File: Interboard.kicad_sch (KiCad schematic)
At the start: 1 part

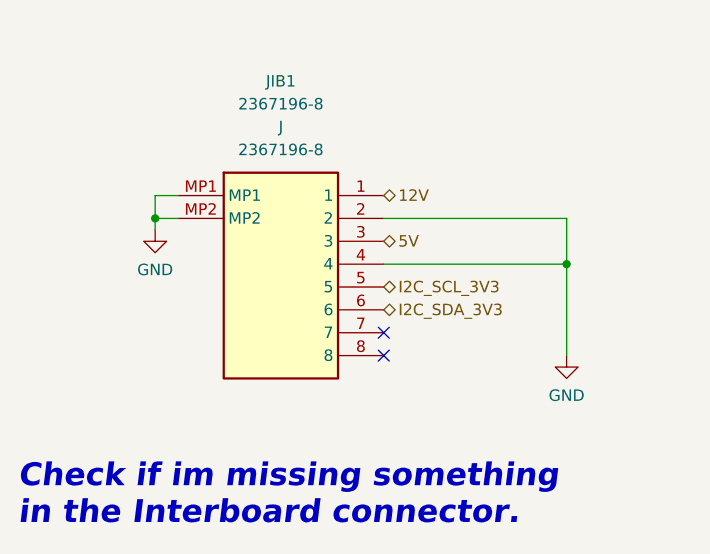
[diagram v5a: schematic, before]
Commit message: Page settings changed. Added some testpoints. Some comments are made.
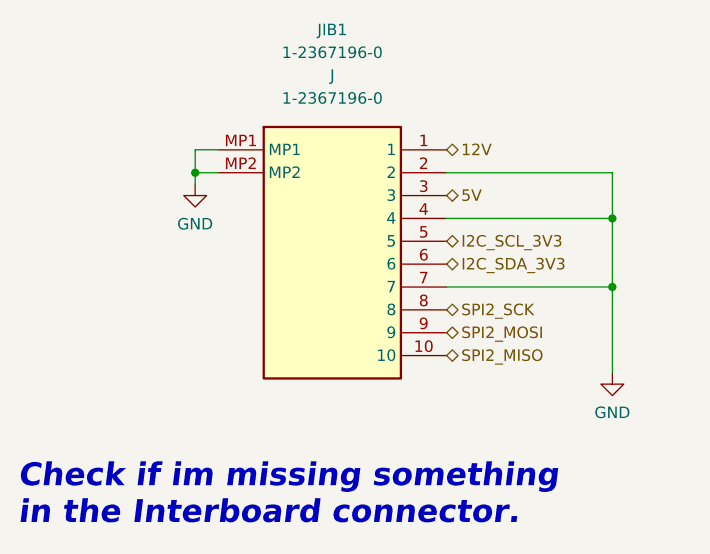
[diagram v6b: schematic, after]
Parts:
- removed JIB1: 2367196-8, symbol 2367196-8:2367196-8
- added JIB1: 1-2367196-0, symbol 1-2367196-0:1-2367196-0
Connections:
- net 12V: now also JIB1.1
- net 5V: now also JIB1.3
- net GND: now also JIB1.2, JIB1.4, JIB1.7, JIB1.MP1, JIB1.MP2
- net I2C_SCL_3V3: now also JIB1.5
- net I2C_SDA_3V3: now also JIB1.6
- new net SPI2_MISO: JIB1.10
- new net SPI2_MOSI: JIB1.9
- new net SPI2_SCK: JIB1.8
- no-connect marks 2 -> 0
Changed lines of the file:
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@@
     (company "Parikshit Student Satellite Team")
   )
-  (junction (at 162.56 86.36) (diameter 0) (color 0 0 0 0)
+  (junction (at 121.285 76.2) (diameter 0) (color 0 0 0 0)
   )
-  (junction (at 116.84 81.28) (diameter 0) (color 0 0 0 0)
+  (junction (at 167.64 88.9) (diameter 0) (color 0 0 0 0)
   )
-  (no_connect (at 142.24 93.98))
-  (no_connect (at 142.24 96.52))
-  (wire (pts (xy 116.84 81.28) (xy 116.84 82.55))
+  (junction (at 167.64 81.28) (diameter 0) (color 0 0 0 0)
+  )
+  (wire (pts (xy 121.285 76.2) (xy 121.285 77.47))
     (stroke (width 0) (type default) (color 0 0 0 0))
   )
-  (wire (pts (xy 119.38 78.74) (xy 116.84 78.74))
+  (wire (pts (xy 149.225 76.2) (xy 167.64 76.2))
     (stroke (width 0) (type default) (color 0 0 0 0))
   )
-  (wire (pts (xy 162.56 81.28) (xy 162.56 86.36))
+  (wire (pts (xy 167.64 76.2) (xy 167.64 81.28))
     (stroke (width 0) (type default) (color 0 0 0 0))
   )
-  (wire (pts (xy 142.24 86.36) (xy 162.56 86.36))
+  (wire (pts (xy 167.64 88.9) (xy 167.64 98.425))
     (stroke (width 0) (type default) (color 0 0 0 0))
   )
-  (wire (pts (xy 116.84 81.28) (xy 119.38 81.28))
+  (wire (pts (xy 167.64 81.28) (xy 167.64 88.9))
     (stroke (width 0) (type default) (color 0 0 0 0))
   )
-  (wire (pts (xy 116.84 78.74) (xy 116.84 81.28))
+  (wire (pts (xy 149.225 81.28) (xy 167.64 81.28))
     (stroke (width 0) (type default) (color 0 0 0 0))
   )
-  (wire (pts (xy 142.24 81.28) (xy 162.56 81.28))
+  (wire (pts (xy 123.825 73.66) (xy 121.285 73.66))
     (stroke (width 0) (type default) (color 0 0 0 0))
   )
-  (wire (pts (xy 162.56 86.36) (xy 162.56 96.52))
+  (wire (pts (xy 121.285 76.2) (xy 123.825 76.2))
+    (stroke (width 0) (type default) (color 0 0 0 0))
+  )
+  (wire (pts (xy 121.285 73.66) (xy 121.285 76.2))
+    (stroke (width 0) (type default) (color 0 0 0 0))
+  )
+  (wire (pts (xy 149.225 88.9) (xy 167.64 88.9))
     (stroke (width 0) (type default) (color 0 0 0 0))
   )
@@
     (effects (font (size 2.54 2.54) (thickness 0.508) bold italic) (justify left bottom))
   )
-  (hierarchical_label "12V" (shape bidirectional) (at 142.24 78.74 0)
+  (hierarchical_label "5V" (shape bidirectional) (at 149.225 78.74 0)
     (effects (font (size 1.27 1.27)) (justify left))
   )
-  (hierarchical_label "I2C_SCL_3V3" (shape bidirectional) (at 142.24 88.9 0)
+  (hierarchical_label "12V" (shape bidirectional) (at 149.225 73.66 0)
     (effects (font (size 1.27 1.27)) (justify left))
   )
-  (hierarchical_label "I2C_SDA_3V3" (shape bidirectional) (at 142.24 91.44 0)
+  (hierarchical_label "I2C_SCL_3V3" (shape bidirectional) (at 149.225 83.82 0)
     (effects (font (size 1.27 1.27)) (justify left))
   )
-  (hierarchical_label "5V" (shape bidirectional) (at 142.24 83.82 0)
+  (hierarchical_label "SPI2_MOSI" (shape bidirectional) (at 149.225 93.98 0)
     (effects (font (size 1.27 1.27)) (justify left))
   )
-  (symbol (lib_id "upsat-comms-hardware:GND") (at 162.56 96.52 0) (unit 1)
+  (hierarchical_label "SPI2_SCK" (shape bidirectional) (at 149.225 91.44 0)
+    (effects (font (size 1.27 1.27)) (justify left))
+  )
+  (hierarchical_label "I2C_SDA_3V3" (shape bidirectional) (at 149.225 86.36 0)
+    (effects (font (size 1.27 1.27)) (justify left))
+  )
+  (hierarchical_label "SPI2_MISO" (shape bidirectional) (at 149.225 96.52 0)
+    (effects (font (size 1.27 1.27)) (justify left))
+  )
+  (symbol (lib_id "1-2367196-0:1-2367196-0") (at 123.825 73.66 0) (unit 1)
     (in_bom yes) (on_board yes) (fields_autoplaced)
-    (property "Reference" "#PWR0149" (id 0) (at 162.56 102.87 0)
+    (property "Reference" "JIB1" (id 0) (at 136.525 60.325 0))
+    (property "Value" "1-2367196-0" (id 1) (at 136.525 62.865 0))
+    (property "Footprint" "" (id 2) (at 123.825 73.66 0)
       (effects (font (size 1.27 1.27)) hide)
     )
-    (property "Value" "GND" (id 1) (at 162.56 100.965 0))
-    (property "Footprint" "" (id 2) (at 162.56 96.52 0))
-    (property "Datasheet" "" (id 3) (at 162.56 96.52 0))
-    (pin "1")
-  )
-  (symbol (lib_id "2367196-8:2367196-8") (at 119.38 78.74 0) (unit 1)
-    (in_bom yes) (on_board yes) (fields_autoplaced)
-    (property "Reference" "JIB1" (id 0) (at 130.81 66.04 0))
-    (property "Value" "2367196-8" (id 1) (at 130.81 68.58 0))
-    (property "Footprint" "" (id 2) (at 119.38 78.74 0)
+    (property "Datasheet" "" (id 3) (at 123.825 73.66 0)
       (effects (font (size 1.27 1.27)) hide)
     )
-    (property "Datasheet" "" (id 3) (at 119.38 78.74 0)
-      (effects (font (size 1.27 1.27)) hide)
-    )
-    (property "Reference_1" "J" (id 4) (at 130.81 71.12 0))
-    (property "Value_1" "2367196-8" (id 5) (at 130.81 73.66 0))
-    (property "Footprint_1" "23671968" (id 6) (at 138.43 173.66 0)
+    (property "Reference_1" "J" (id 4) (at 136.525 65.405 0))
+    (property "Value_1" "1-2367196-0" (id 5) (at 136.525 67.945 0))
+    (property "Footprint_1" "123671960" (id 6) (at 145.415 168.58 0)
       (effects (font (size 1.27 1.27)) (justify left top) hide)
     )
-    (property "Datasheet_1" "https://www.te.com/commerce/DocumentDelivery/DDEController?Action=showdoc&DocId=Customer+Drawing%7F2367196%7FA%7Fpdf%7FEnglish%7FENG_CD_2367196_A.pdf%7F2367196-8" (id 7) (at 138.43 273.66 0)
+    (property "Datasheet_1" "https://www.te.com/commerce/DocumentDelivery/DDEController?Action=showdoc&DocId=Customer+Drawing%7F2367196%7FA%7Fpdf%7FEnglish%7FENG_CD_2367196_A.pdf%7F1-2367196-0" (id 7) (at 145.415 268.58 0)
       (effects (font (size 1.27 1.27)) (justify left top) hide)
     )
-    (property "Height" "3.25" (id 8) (at 138.43 473.66 0)
+    (property "Height" "3.65" (id 8) (at 145.415 468.58 0)
       (effects (font (size 1.27 1.27)) (justify left top) hide)
     )
-    (property "Mouser Part Number" "571-2367196-8" (id 9) (at 138.43 573.66 0)
+    (property "Mouser Part Number" "571-1-2367196-0" (id 9) (at 145.415 568.58 0)
       (effects (font (size 1.27 1.27)) (justify left top) hide)
     )
-    (property "Mouser Price/Stock" "https://www.mouser.co.uk/ProductDetail/TE-Connectivity/2367196-8?qs=sPbYRqrBIVndDqCjm2TjhA%3D%3D" (id 10) (at 138.43 673.66 0)
+    (property "Mouser Price/Stock" "https://www.mouser.co.uk/ProductDetail/TE-Connectivity/1-2367196-0?qs=sPbYRqrBIVnEArKS36KmYQ%3D%3D" (id 10) (at 145.415 668.58 0)
       (effects (font (size 1.27 1.27)) (justify left top) hide)
     )
-    (property "Manufacturer_Name" "TE Connectivity" (id 11) (at 138.43 773.66 0)
+    (property "Manufacturer_Name" "TE Connectivity" (id 11) (at 145.415 768.58 0)
       (effects (font (size 1.27 1.27)) (justify left top) hide)
     )
-    (property "Manufacturer_Part_Number" "2367196-8" (id 12) (at 138.43 873.66 0)
+    (property "Manufacturer_Part_Number" "1-2367196-0" (id 12) (at 145.415 868.58 0)
       (effects (font (size 1.27 1.27)) (justify left top) hide)
     )
     (pin "1")
+    (pin "10")
     (pin "2")
     (pin "3")
@@
     (pin "7")
     (pin "8")
+    (pin "9")
     (pin "MP1")
     (pin "MP2")
   )
-  (symbol (lib_id "upsat-comms-hardware:GND") (at 116.84 82.55 0) (unit 1)
+  (symbol (lib_id "upsat-comms-hardware:GND") (at 121.285 77.47 0) (unit 1)
     (in_bom yes) (on_board yes) (fields_autoplaced)
-    (property "Reference" "#PWR0148" (id 0) (at 116.84 88.9 0)
+    (property "Reference" "#PWR0161" (id 0) (at 121.285 83.82 0)
       (effects (font (size 1.27 1.27)) hide)
     )
-    (property "Value" "GND" (id 1) (at 116.84 86.995 0))
-    (property "Footprint" "" (id 2) (at 116.84 82.55 0))
-    (property "Datasheet" "" (id 3) (at 116.84 82.55 0))
+    (property "Value" "GND" (id 1) (at 121.285 81.915 0))
+    (property "Footprint" "" (id 2) (at 121.285 77.47 0))
+    (property "Datasheet" "" (id 3) (at 121.285 77.47 0))
     (pin "1")
   )
+  (symbol (lib_id "upsat-comms-hardware:GND") (at 167.64 98.425 0) (unit 1)
+    (in_bom yes) (on_board yes) (fields_autoplaced)
+    (property "Reference" "#PWR0162" (id 0) (at 167.64 104.775 0)
+      (effects (font (size 1.27 1.27)) hide)
+    )
+    (property "Value" "GND" (id 1) (at 167.64 102.87 0))
+    (property "Footprint" "" (id 2) (at 167.64 98.425 0))
+    (property "Datasheet" "" (id 3) (at 167.64 98.425 0))
+    (pin "1")
+  )

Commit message: FInal comments
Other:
- note added: "Chinmay : CHcek if theres a 4th line for SPI"
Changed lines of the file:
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@@
     (effects (font (size 2.54 2.54) (thickness 0.508) bold italic) (justify left bottom))
+  )
+  (text "Chinmay : CHcek if theres a 4th line for SPI " (at 165.1 66.04 0)
+    (effects (font (size 1.27 1.27)) (justify left bottom))
   )
   (hierarchical_label "5V" (shape bidirectional) (at 149.225 78.74 0)
